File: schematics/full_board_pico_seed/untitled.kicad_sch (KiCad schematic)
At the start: 10 parts, among them J6 Conn_01x03_Female, U10 LM4881M/NOPB

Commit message: worked on schematics
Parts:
- J6: now left out of the parts list
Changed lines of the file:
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@@
 		(shape input)
 		(at 177.8 46.99 0)
-		(fields_autoplaced yes)
 		(effects
 			(font
@@
 		(shape input)
 		(at 87.63 59.69 180)
-		(fields_autoplaced yes)
 		(effects
 			(font
@@
 		(unit 1)
 		(exclude_from_sim no)
-		(in_bom yes)
-		(on_board yes)
-		(dnp no)
+		(in_bom no)
+		(on_board yes)
+		(dnp no)

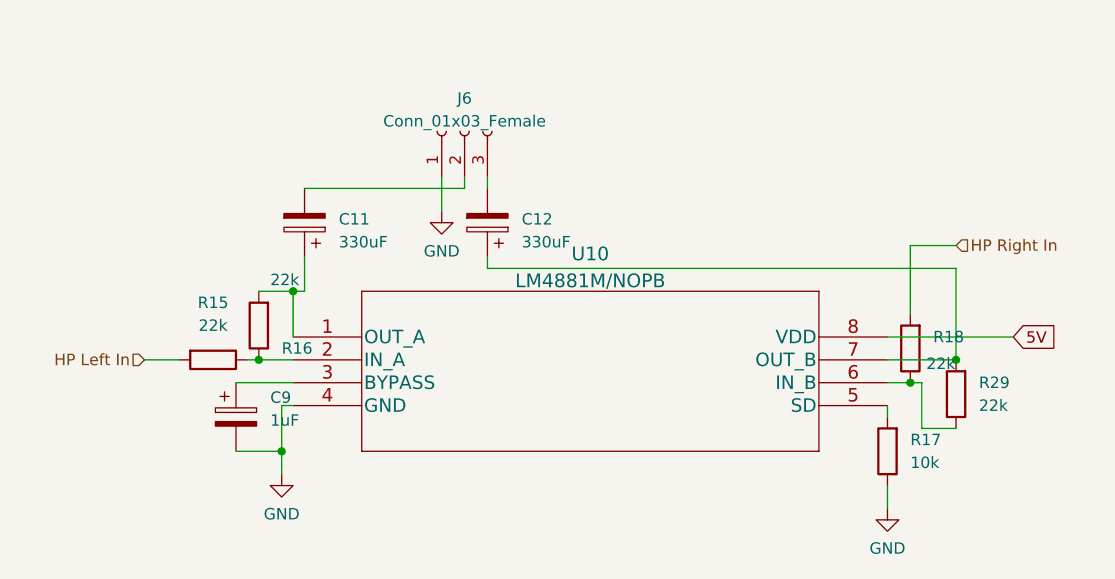
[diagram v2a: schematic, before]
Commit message: corrected schematic regarding pcm3060
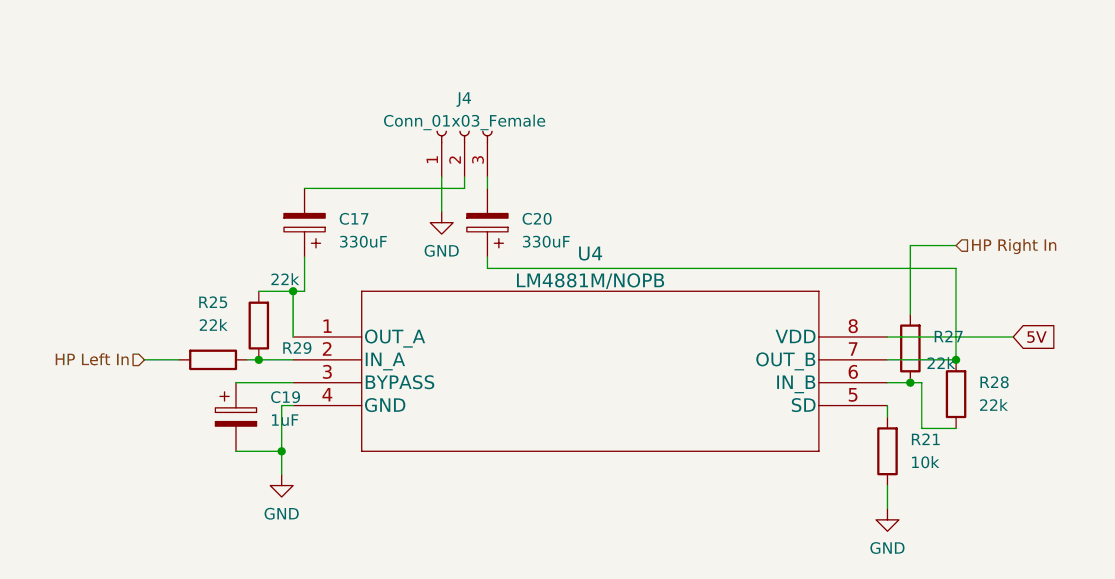
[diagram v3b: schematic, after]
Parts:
- renumbered C11 to C17, C9 to C19, C12 to C20, J6 to J4, R17 to R21, R15 to R25, R18 to R27, R29 to R28, R16 to R29, U10 to U4
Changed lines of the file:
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@@
 		(dnp no)
 		(fields_autoplaced yes)
-		(property "Reference" "R15"
+		(property "Reference" "R25"
 			(at 95.25 53.34 90)
 			(effects
@@
 			(project "full_board_pico_seed"
 				(path "/e63e39d7-6ac0-4ffd-8aa3-1841a4541b55/5b76a2fc-3494-4cf0-b601-f44157bc070a"
-					(reference "R15")
+					(reference "R25")
 					(unit 1)
 				)
@@
 		(dnp no)
 		(fields_autoplaced yes)
-		(property "Reference" "U10"
+		(property "Reference" "U4"
 			(at 137.16 47.9224 0)
 			(effects
@@
 			(project "full_board_pico_seed"
 				(path "/e63e39d7-6ac0-4ffd-8aa3-1841a4541b55/5b76a2fc-3494-4cf0-b601-f44157bc070a"
-					(reference "U10")
+					(reference "U4")
 					(unit 1)
 				)
@@
 		(on_board yes)
 		(dnp no)
-		(property "Reference" "R18"
+		(property "Reference" "R27"
 			(at 175.26 57.15 0)
 			(effects
@@
 			(project "full_board_pico_seed"
 				(path "/e63e39d7-6ac0-4ffd-8aa3-1841a4541b55/5b76a2fc-3494-4cf0-b601-f44157bc070a"
-					(reference "R18")
+					(reference "R27")
 					(unit 1)
 				)
@@
 		(on_board yes)
 		(dnp no)
-		(property "Reference" "R16"
+		(property "Reference" "R29"
 			(at 102.87 58.42 0)
 			(effects
@@
 			(project "full_board_pico_seed"
 				(path "/e63e39d7-6ac0-4ffd-8aa3-1841a4541b55/5b76a2fc-3494-4cf0-b601-f44157bc070a"
-					(reference "R16")
+					(reference "R29")
 					(unit 1)
 				)
@@
 		(dnp no)
 		(fields_autoplaced yes)
-		(property "Reference" "R17"
+		(property "Reference" "R21"
 			(at 172.72 68.58 0)
 			(effects
@@
 			(project "full_board_pico_seed"
 				(path "/e63e39d7-6ac0-4ffd-8aa3-1841a4541b55/5b76a2fc-3494-4cf0-b601-f44157bc070a"
-					(reference "R17")
+					(reference "R21")
 					(unit 1)
 				)
@@
 		(dnp no)
 		(fields_autoplaced yes)
-		(property "Reference" "J6"
+		(property "Reference" "J4"
 			(at 123.19 30.641 90)
 			(effects
@@
 			(project "full_board_pico_seed"
 				(path "/e63e39d7-6ac0-4ffd-8aa3-1841a4541b55/5b76a2fc-3494-4cf0-b601-f44157bc070a"
-					(reference "J6")
+					(reference "J4")
 					(unit 1)
 				)
@@
 		(dnp no)
 		(fields_autoplaced yes)
-		(property "Reference" "C11"
+		(property "Reference" "C17"
 			(at 109.22 44.069 0)
 			(effects
@@
 			(project "full_board_pico_seed"
 				(path "/e63e39d7-6ac0-4ffd-8aa3-1841a4541b55/5b76a2fc-3494-4cf0-b601-f44157bc070a"
-					(reference "C11")
+					(reference "C17")
 					(unit 1)
 				)
@@
 		(dnp no)
 		(fields_autoplaced yes)
-		(property "Reference" "C12"
+		(property "Reference" "C20"
 			(at 129.54 44.069 0)
 			(effects
@@
 			(project "full_board_pico_seed"
 				(path "/e63e39d7-6ac0-4ffd-8aa3-1841a4541b55/5b76a2fc-3494-4cf0-b601-f44157bc070a"
-					(reference "C12")
+					(reference "C20")
 					(unit 1)
 				)
@@
 		(dnp no)
 		(fields_autoplaced yes)
-		(property "Reference" "C9"
+		(property "Reference" "C19"
 			(at 101.6 63.881 0)
 			(effects
@@
 			(project "full_board_pico_seed"
 				(path "/e63e39d7-6ac0-4ffd-8aa3-1841a4541b55/5b76a2fc-3494-4cf0-b601-f44157bc070a"
-					(reference "C9")
+					(reference "C19")
 					(unit 1)
 				)
@@
 		(dnp no)
 		(fields_autoplaced yes)
-		(property "Reference" "R29"
+		(property "Reference" "R28"
 			(at 180.34 62.23 0)
 			(effects
@@
 			(project "full_board_pico_seed"
 				(path "/e63e39d7-6ac0-4ffd-8aa3-1841a4541b55/5b76a2fc-3494-4cf0-b601-f44157bc070a"
-					(reference "R29")
-					(unit 1)
-				)
+					(reference "R28")
+					(unit 1)
+				)

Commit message: schematic change
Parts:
- renumbered C17 to C16, C19 to C17, C20 to C19, J4 to J5, R28 to R21, R29 to R22, R21 to R23, R27 to R24
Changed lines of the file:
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@@
 		(on_board yes)
 		(dnp no)
-		(fields_autoplaced yes)
 		(property "Reference" "R25"
-			(at 95.25 53.34 90)
+			(at 95.25 55.118 90)
 			(effects
 				(font
@@
 		)
 		(property "Value" "22k"
-			(at 95.25 55.88 90)
+			(at 95.25 57.404 90)
 			(effects
 				(font
@@
 		(on_board yes)
 		(dnp no)
-		(property "Reference" "R27"
+		(property "Reference" "R24"
 			(at 175.26 57.15 0)
 			(effects
@@
 			(project "full_board_pico_seed"
 				(path "/e63e39d7-6ac0-4ffd-8aa3-1841a4541b55/5b76a2fc-3494-4cf0-b601-f44157bc070a"
-					(reference "R27")
+					(reference "R24")
 					(unit 1)
 				)
@@
 		(on_board yes)
 		(dnp no)
-		(property "Reference" "R29"
-			(at 102.87 58.42 0)
+		(property "Reference" "R22"
+			(at 102.616 56.134 0)
 			(effects
 				(font
@@
 		)
 		(property "Value" "22k"
-			(at 101.6 50.8 0)
+			(at 102.616 54.102 0)
 			(effects
 				(font
@@
 			(project "full_board_pico_seed"
 				(path "/e63e39d7-6ac0-4ffd-8aa3-1841a4541b55/5b76a2fc-3494-4cf0-b601-f44157bc070a"
-					(reference "R29")
+					(reference "R22")
 					(unit 1)
 				)
@@
 		(dnp no)
 		(fields_autoplaced yes)
-		(property "Reference" "R21"
+		(property "Reference" "R23"
 			(at 172.72 68.58 0)
 			(effects
@@
 			(project "full_board_pico_seed"
 				(path "/e63e39d7-6ac0-4ffd-8aa3-1841a4541b55/5b76a2fc-3494-4cf0-b601-f44157bc070a"
-					(reference "R21")
+					(reference "R23")
 					(unit 1)
 				)
@@
 		(dnp no)
 		(fields_autoplaced yes)
-		(property "Reference" "J4"
+		(property "Reference" "J5"
 			(at 123.19 30.641 90)
 			(effects
@@
 			(project "full_board_pico_seed"
 				(path "/e63e39d7-6ac0-4ffd-8aa3-1841a4541b55/5b76a2fc-3494-4cf0-b601-f44157bc070a"
-					(reference "J4")
+					(reference "J5")
 					(unit 1)
 				)
@@
 		(dnp no)
 		(fields_autoplaced yes)
-		(property "Reference" "C17"
+		(property "Reference" "C16"
 			(at 109.22 44.069 0)
 			(effects
@@
 			(project "full_board_pico_seed"
 				(path "/e63e39d7-6ac0-4ffd-8aa3-1841a4541b55/5b76a2fc-3494-4cf0-b601-f44157bc070a"
-					(reference "C17")
+					(reference "C16")
 					(unit 1)
 				)
@@
 		(dnp no)
 		(fields_autoplaced yes)
-		(property "Reference" "C20"
+		(property "Reference" "C19"
 			(at 129.54 44.069 0)
 			(effects
@@
 			(project "full_board_pico_seed"
 				(path "/e63e39d7-6ac0-4ffd-8aa3-1841a4541b55/5b76a2fc-3494-4cf0-b601-f44157bc070a"
-					(reference "C20")
+					(reference "C19")
 					(unit 1)
 				)
@@
 		(dnp no)
 		(fields_autoplaced yes)
-		(property "Reference" "C19"
+		(property "Reference" "C17"
 			(at 101.6 63.881 0)
 			(effects
@@
 			(project "full_board_pico_seed"
 				(path "/e63e39d7-6ac0-4ffd-8aa3-1841a4541b55/5b76a2fc-3494-4cf0-b601-f44157bc070a"
-					(reference "C19")
+					(reference "C17")
 					(unit 1)
 				)
@@
 		(dnp no)
 		(fields_autoplaced yes)
-		(property "Reference" "R28"
+		(property "Reference" "R21"
 			(at 180.34 62.23 0)
 			(effects
@@
 			(project "full_board_pico_seed"
 				(path "/e63e39d7-6ac0-4ffd-8aa3-1841a4541b55/5b76a2fc-3494-4cf0-b601-f44157bc070a"
-					(reference "R28")
-					(unit 1)
-				)
+					(reference "R21")
+					(unit 1)
+				)

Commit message: updated schematic
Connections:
- net at J5.2 (Pin_2): now also C19.2; no longer C16.2
- net at J5.3 (Pin_3): now also C16.2; no longer C19.2
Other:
- moved on the sheet: J5
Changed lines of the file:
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@@
+	(wire
+		(pts
+			(xy 123.19 40.64) (xy 123.19 31.75)
+		)
+		(stroke
+			(width 0)
+			(type default)
+		)
+	)
 	(wire
 		(pts
@@
 	(wire
 		(pts
-			(xy 105.41 40.64) (xy 123.19 40.64)
-		)
-		(stroke
-			(width 0)
-			(type default)
-		)
-	)
-	(wire
-		(pts
 			(xy 172.72 46.99) (xy 177.8 46.99)
 		)
@@
 	(wire
 		(pts
-			(xy 125.73 40.64) (xy 125.73 39.37)
+			(xy 125.73 40.64) (xy 123.19 40.64)
 		)
 		(stroke
@@
 	(wire
 		(pts
-			(xy 123.19 40.64) (xy 123.19 39.37)
-		)
-		(stroke
-			(width 0)
-			(type default)
-		)
-	)
-	(wire
-		(pts
 			(xy 177.8 59.69) (xy 177.8 49.53)
 		)
@@
 	(wire
 		(pts
-			(xy 120.65 39.37) (xy 120.65 43.18)
+			(xy 120.65 31.75) (xy 120.65 43.18)
+		)
+		(stroke
+			(width 0)
+			(type default)
+		)
+	)
+	(wire
+		(pts
+			(xy 105.41 34.29) (xy 125.73 34.29)
+		)
+		(stroke
+			(width 0)
+			(type default)
+		)
+	)
+	(wire
+		(pts
+			(xy 105.41 40.64) (xy 105.41 34.29)
+		)
+		(stroke
+			(width 0)
+			(type default)
+		)
+	)
+	(wire
+		(pts
+			(xy 125.73 34.29) (xy 125.73 31.75)
 		)
 		(stroke
@@
 	(symbol
 		(lib_id "Connector:Conn_01x03_Female")
-		(at 123.19 34.29 90)
+		(at 123.19 26.67 90)
 		(unit 1)
 		(exclude_from_sim no)
@@
 		(fields_autoplaced yes)
 		(property "Reference" "J5"
-			(at 123.19 30.641 90)
+			(at 123.19 23.021 90)
 			(effects
 				(font
@@
 		)
 		(property "Value" "Conn_01x03_Female"
-			(at 123.19 33.1779 90)
+			(at 123.19 25.5579 90)
 			(effects
 				(font
@@
 		)
 		(property "Footprint" "Connector_PinHeader_2.54mm:PinHeader_1x03_P2.54mm_Vertical"
-			(at 123.19 34.29 0)
+			(at 123.19 26.67 0)
 			(effects
 				(font
@@
 		)
 		(property "Datasheet" "~"
-			(at 123.19 34.29 0)
+			(at 123.19 26.67 0)
 			(effects
 				(font
@@
 		)
 		(property "Description" ""
-			(at 123.19 34.29 0)
-			(effects
-				(font
+			(at 123.19 26.67 0)
+			(effects
+				(font
